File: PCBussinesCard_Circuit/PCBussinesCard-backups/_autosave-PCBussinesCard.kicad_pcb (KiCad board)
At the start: 2 copper layers, 85 x 55 mm, 18 parts, among them IC1 NT2H1311F0DTL, J1 Conn_ARM_JTAG_SWD_10, J2 USB_A_PCB, J3 Conn_01x13_Pin, J4 Conn_01x13_Pin, U1 STM32L552CCTx, U2 AP7370-33FDC

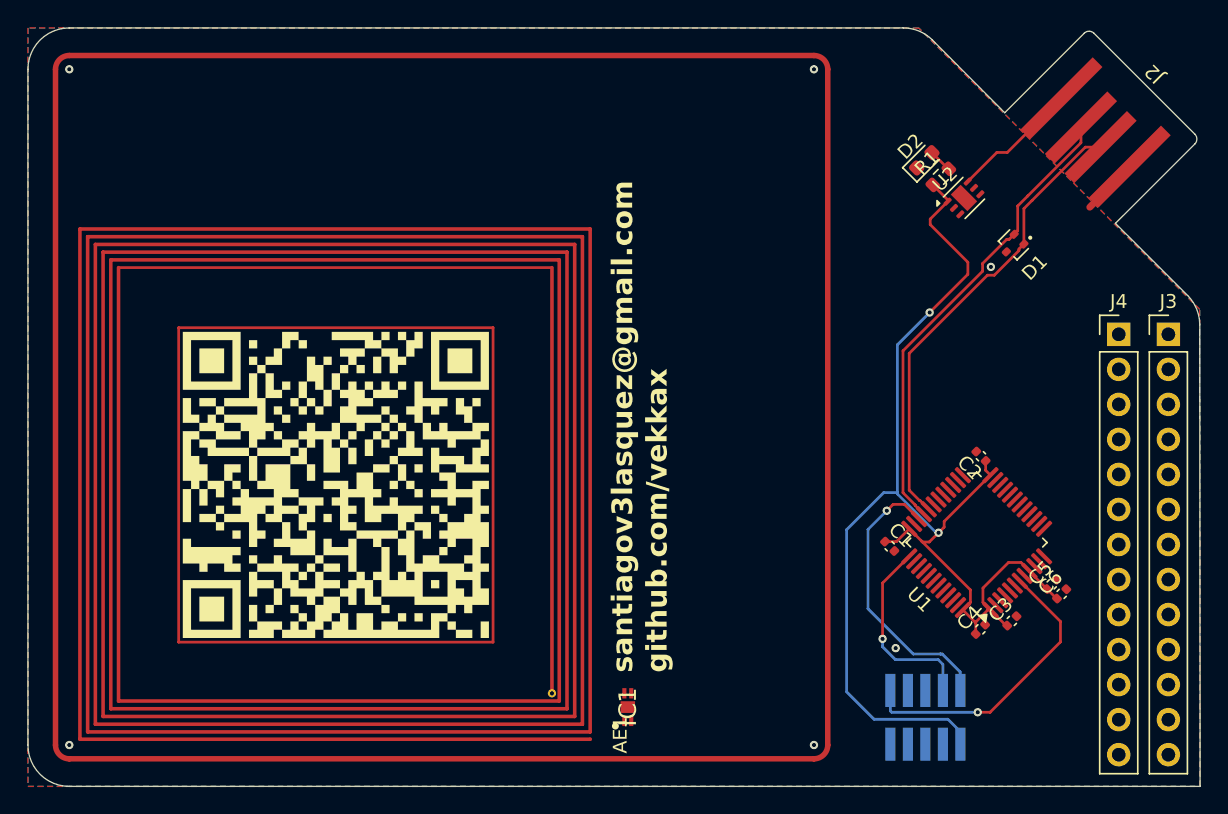
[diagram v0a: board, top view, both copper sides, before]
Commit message: provisional antena added
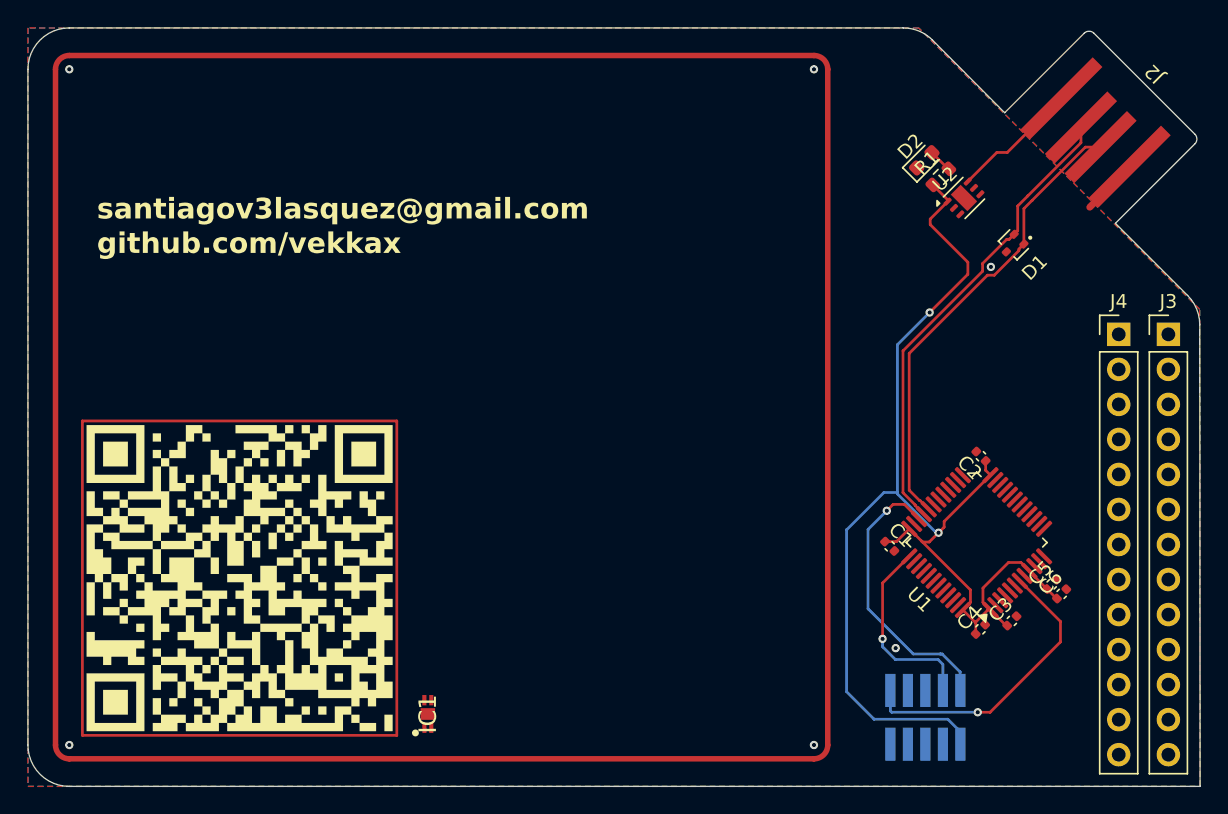
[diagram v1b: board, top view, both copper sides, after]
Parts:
- removed AE1: Ntag_Antenna, ProjectLibrary:Ntag_Antenna
- moved IC1 14.5 mm to (129.0, 124.8)
- moved G*** 9.72 mm to (115.3, 114.9)
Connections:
- IC1 pad 2: Net-(IC1-LB) -> unconnected-(IC1-LB-Pad2)
- IC1 pad 3: Net-(IC1-FD) -> unconnected-(IC1-FD-Pad3)
